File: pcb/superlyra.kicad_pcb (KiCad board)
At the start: 2 copper layers, 391.1 x 134.8 mm, 223 parts, among them J1 USB_C_Receptacle_USB2.0, J2 AVR-ISP-6, SW1 SW_Push, SW10 SW_Push, SW11 SW_Push, SW12 SW_Push, SW13 SW_Push, SW14 SW_Push, SW15 SW_Push, SW16 SW_Push, SW17 SW_Push, SW18 SW_Push, SW19 SW_Push, SW2 SW_Push, SW20 SW_Push, SW21 SW_Push, SW22 SW_Push, SW23 SW_Push, SW24 SW_Push, SW25 SW_Push, SW26 SW_Push, SW27 SW_Push, SW28 SW_Push, SW29 SW_Push, SW3 SW_Push, SW30 SW_Push, SW31 SW_Push, SW32 SW_Push, SW33 SW_Push, SW34 SW_Push, SW35 SW_Push, SW36 SW_Push, SW37 SW_Push, SW38 SW_Push, SW39 SW_Push, SW4 SW_Push, SW40 SW_Push, SW41 SW_Push, SW42 SW_Push, SW43 SW_Push, SW44 SW_Push, SW45 SW_Push, SW46 SW_Push, SW47 SW_Push, SW48 SW_Push, SW49 SW_Push, SW5 SW_Push, SW50 SW_Push, SW51 SW_Push, SW52 SW_Push, SW53 SW_Push, SW54 SW_Push, SW55 SW_Push, SW56 SW_Push, SW57 SW_Push, SW58 SW_Push, SW59 SW_Push, SW6 SW_Push, SW60 SW_Push, SW61 SW_Push, SW62 SW_Push, SW63 SW_Push, SW64 SW_Push, SW65 SW_Push, SW66 SW_Push, SW67 SW_Push, SW68 SW_Push, SW69 SW_Push, SW7 SW_Push, SW70 SW_Push, SW71 SW_Push, SW72 SW_Push, SW73 SW_Push, SW74 SW_Push, SW75 SW_Push, SW76 SW_Push, SW77 SW_Push, SW78 SW_Push, SW79 SW_Push, SW8 SW_Push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

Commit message: 0.5 (evaluation)
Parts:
- removed G***: LOGO, gfx:SuperLyraLogo
- removed REF** (x23): MountingHole_2.1mm, MountingHole:MountingHole_2.1mm
- removed the SW85 at (297.0, 165.2)
- added C6: 0.1u, Keebio:C_0402, F.Cu at (232.3, 87.1)
- added H1: MountingHole, MountingHole:MountingHole_2.2mm_M2_ISO7380_Pad, F.Cu at (59.7, 68.8)
- added H10: MountingHole, MountingHole:MountingHole_2.2mm_M2_ISO7380_Pad, F.Cu at (165.7, 84.3)
- added H11: MountingHole, MountingHole:MountingHole_2.2mm_M2_ISO7380_Pad, F.Cu at (256.4, 84.1)
- added H12: MountingHole, MountingHole:MountingHole_2.2mm_M2_ISO7380_Pad, F.Cu at (252.0, 121.3)
- added H13: MountingHole, MountingHole:MountingHole_2.2mm_M2_ISO7380_Pad, F.Cu at (255.4, 156.8)
- added H14: MountingHole, MountingHole:MountingHole_2.2mm_M2_ISO7380_Pad, F.Cu at (323.3, 78.9)
- added H15: MountingHole, MountingHole:MountingHole_2.2mm_M2_ISO7380_Pad, F.Cu at (247.9, 187.2)
- added H16: MountingHole, MountingHole:MountingHole_2.2mm_M2_ISO7380_Pad, F.Cu at (308.4, 170.8)
- added H17: MountingHole, MountingHole:MountingHole_2.2mm_M2_ISO7380_Pad, F.Cu at (335.3, 125.1)
- added H18: MountingHole, MountingHole:MountingHole_2.2mm_M2_ISO7380_Pad, F.Cu at (191.0, 142.1)
- added H19: MountingHole, MountingHole:MountingHole_2.2mm_M2_ISO7380_Pad, F.Cu at (291.7, 108.2)
- added H2: MountingHole, MountingHole:MountingHole_2.2mm_M2_ISO7380_Pad, F.Cu at (37.1, 153.9)
- added H20: MountingHole, MountingHole:MountingHole_2.2mm_M2_ISO7380_Pad, F.Cu at (360.4, 69.6)
- added H21: MountingHole, MountingHole:MountingHole_2.2mm_M2_ISO7380_Pad, F.Cu at (209.9, 163.6)
- added H22: MountingHole, MountingHole:MountingHole_2.2mm_M2_ISO7380_Pad, F.Cu at (229.1, 142.0)
- added H23: MountingHole, MountingHole:MountingHole_2.2mm_M2_ISO7380_Pad, F.Cu at (382.9, 154.7)
- added H24: MountingHole, MountingHole:MountingHole_2.2mm_M2_ISO7380_Pad, F.Cu at (209.9, 125.6)
- added H25: Logo, gfx:SuperLyraLogo, F.Cu at (181.4, 84.3)
- added H3: MountingHole, MountingHole:MountingHole_2.2mm_M2_ISO7380_Pad, F.Cu at (96.5, 79.5)
- added H4: MountingHole, MountingHole:MountingHole_2.2mm_M2_ISO7380_Pad, F.Cu at (84.8, 125.2)
- added H5: MountingHole, MountingHole:MountingHole_2.2mm_M2_ISO7380_Pad, F.Cu at (111.0, 170.4)
- added H6: MountingHole, MountingHole:MountingHole_2.2mm_M2_ISO7380_Pad, F.Cu at (128.0, 108.2)
- added H7: MountingHole, MountingHole:MountingHole_2.2mm_M2_ISO7380_Pad, F.Cu at (168.0, 121.2)
- added H8: MountingHole, MountingHole:MountingHole_2.2mm_M2_ISO7380_Pad, F.Cu at (165.0, 156.6)
- added H9: MountingHole, MountingHole:MountingHole_2.2mm_M2_ISO7380_Pad, F.Cu at (172.0, 187.3)
- D1, D10, D11, D12, D13, D14, D15, D16, D17, D18, D19, D2, D20, D21, D22, D23, D24, D25, D26, D27, D28, D29, D3, D30, D31, D32, D33, D34, D35, D36, D37, D38, D39, D4, D40, D41, D42, D43, D44, D45, D46, D47, D48, D49, D5, D50, D51, D52, D53, D54, D55, D56, D57, D58, D59, D6, D60, D61, D62, D63, D64, D65, D66, D67, D68, D69, D7, D70, D71, D72, D73, D74, D75, D76, D77, D78, D79, D8, D80, D81, D82, D83, D84, D85, D86, D87, D88, D89, D9, D90: footprint Keebio:D_0805 -> Diode_SMD:D_SOD-123F
- F1: footprint Fuse:Fuse_1206_3216Metric -> Fuse:Fuse_0402_1005Metric
- Y1: footprint Crystal:Resonator_SMD_muRata_CSTxExxV-3Pin_3.0x1.1mm_HandSoldering -> Crystal:Resonator_SMD_muRata_CSTxExxV-3Pin_3.0x1.1mm
- moved F1 19.3 mm to (228.6, 80.8)
- moved C1 8.62 mm to (235.7, 78.2), turned to 90 degrees
- moved R2 7.64 mm to (232.2, 79.2)
- moved R1 7.64 mm to (232.2, 80.3)
- moved C2 6.11 mm to (237.5, 78.2), turned to 90 degrees
- moved R3 5.30 mm to (231.1, 86.0)
- moved C3 5.18 mm to (243.6, 85.1), turned to 0 degrees
- moved D3 4.71 mm to (94.1, 88.5), turned to 75 degrees
- moved R4 4.66 mm to (243.6, 86.1), turned to 180 degrees
- moved C5 4.23 mm to (232.2, 81.5), turned to 180 degrees
- moved U2 3.84 mm to (218.4, 82.3), turned to 0 degrees
- moved J2 3.81 mm to (198.4, 83.3), turned to 180 degrees
- moved D21 3.42 mm to (92.8, 93.1), turned to 255 degrees
- moved C4 3.39 mm to (237.5, 90.2)
- moved D12 3.20 mm to (270.1, 101.8), turned to 105 degrees
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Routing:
- net GND: track 88.7 -> 43.5 mm, vias 34 -> 17
- net COL16: track 183.9 -> 150.0 mm
- net COL15: track 165.6 -> 133.2 mm
- net ROW3: track 520.8 -> 491.1 mm, vias 4 -> 3
- net MISO: track 469.7 -> 443.0 mm, vias 4 -> 2
- net MOSI: track 490.4 -> 467.6 mm
- net COL11: track 99.2 -> 79.8 mm
- net ROW0: track 402.5 -> 386.0 mm
- net COL14: track 143.2 -> 128.2 mm
- net /D-: track 18.9 -> 4.23 mm
- net /D+: track 18.4 -> 3.86 mm
- net COL13: track 120.6 -> 107.1 mm
- net /vbus-in: track 14.8 -> 26.6 mm, vias 0 -> 2
- net Net-(C1-Pad1): track 15.2 -> 5.69 mm
- net Net-(D12-Pad2): track 20.2 -> 11.1 mm
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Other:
- board text added: "github.com/Malevolti/SuperLyra ver. 0.5 (evaluation) youtu.be/8CP6Chss0y0"
- board text removed: "github.com/Malevolti/SuperLyra ver. 1.0 youtu.be/8CP6Chss0y0 Special thanks to Pat for know more about capacitors than me."

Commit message: Update superlyra.kicad_pcb
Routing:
- net VCC: track 110.5 -> 108.0 mm
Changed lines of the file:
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@@
     (thickness 1.6)
     (drawings 20)
-    (tracks 1141)
+    (tracks 1136)
     (zones 0)
     (modules 224)
@@
     (tags "resistor handsolder")
     (attr smd)
-    (fp_text reference R3 (at 0 0.889 90) (layer F.SilkS)
+    (fp_text reference R3 (at -1.651 0 180) (layer F.SilkS)
       (effects (font (size 0.7 0.7) (thickness 0.15)))
     )
@@
     (tags "resistor handsolder")
     (attr smd)
-    (fp_text reference R4 (at 0 -1.17) (layer F.SilkS)
-      (effects (font (size 1 1) (thickness 0.15)))
+    (fp_text reference R4 (at 0 -1.143) (layer F.SilkS)
+      (effects (font (size 0.7 0.7) (thickness 0.15)))
     )
     (fp_text value 10k (at 0 1.17) (layer F.Fab)
@@
     (tags "capacitor 0402")
     (attr smd)
-    (fp_text reference C6 (at 0 -1.016 90) (layer F.SilkS)
+    (fp_text reference C6 (at 1.651 0 180) (layer F.SilkS)
       (effects (font (size 0.7 0.7) (thickness 0.15)))
     )
@@
   (segment (start 233.33668 86.614) (end 232.198 86.614) (width 0.25) (layer F.Cu) (net 3))
   (segment (start 234.069371 85.881309) (end 233.33668 86.614) (width 0.25) (layer F.Cu) (net 3))
-  (segment (start 227.584 82.296) (end 220.98 82.296) (width 0.25) (layer B.Cu) (net 3))
   (segment (start 220.98 82.296) (end 220.98 82.296) (width 0.25) (layer B.Cu) (net 3))
   (via (at 220.98 82.296) (size 0.8) (drill 0.4) (layers F.Cu B.Cu) (net 3))
@@
   (segment (start 235.204 90.17) (end 234.78 90.17) (width 0.25) (layer B.Cu) (net 3))
   (segment (start 239.014 90.17) (end 235.204 90.17) (width 0.25) (layer B.Cu) (net 3))
-  (segment (start 239.48 78.782) (end 238.676 77.978) (width 0.25) (layer B.Cu) (net 3))
-  (segment (start 238.676 77.978) (end 231.902 77.978) (width 0.25) (layer B.Cu) (net 3))
-  (segment (start 230.632 79.248) (end 231.775 78.105) (width 0.25) (layer B.Cu) (net 3))
-  (segment (start 231.775 78.105) (end 231.902 77.978) (width 0.25) (layer B.Cu) (net 3))
-  (segment (start 228.219 80.518) (end 228.219 81.661) (width 0.25) (layer B.Cu) (net 3))
-  (segment (start 228.219 80.518) (end 228.219 79.248) (width 0.25) (layer B.Cu) (net 3))
-  (segment (start 228.219 79.248) (end 230.632 79.248) (width 0.25) (layer B.Cu) (net 3))
-  (segment (start 227.584 82.296) (end 228.219 82.296) (width 0.25) (layer B.Cu) (net 3))
-  (segment (start 228.219 81.661) (end 228.219 82.296) (width 0.25) (layer B.Cu) (net 3))
-  (segment (start 228.219 82.296) (end 228.219 82.804) (width 0.25) (layer B.Cu) (net 3))
-  (segment (start 228.219 82.804) (end 228.219 83.058) (width 0.25) (layer B.Cu) (net 3))
   (segment (start 231.1445 86.572) (end 231.14 86.5765) (width 0.25) (layer F.Cu) (net 3))
   (segment (start 232.283 86.572) (end 231.1445 86.572) (width 0.25) (layer F.Cu) (net 3))
   (segment (start 230.0345 86.5765) (end 229.997 86.614) (width 0.25) (layer F.Cu) (net 3))
   (segment (start 231.14 86.5765) (end 230.0345 86.5765) (width 0.25) (layer F.Cu) (net 3))
-  (segment (start 229.997 86.614) (end 231.521 86.614) (width 0.25) (layer B.Cu) (net 3))
-  (segment (start 231.521 86.614) (end 232.156 85.979) (width 0.25) (layer B.Cu) (net 3))
-  (segment (start 232.156 85.979) (end 232.156 84.709) (width 0.25) (layer B.Cu) (net 3))
-  (segment (start 232.156 84.709) (end 231.648 84.201) (width 0.25) (layer B.Cu) (net 3))
-  (segment (start 229.235 84.201) (end 228.219 83.185) (width 0.25) (layer B.Cu) (net 3))
-  (segment (start 231.648 84.201) (end 229.235 84.201) (width 0.25) (layer B.Cu) (net 3))
-  (segment (start 228.219 82.804) (end 228.219 83.185) (width 0.25) (layer B.Cu) (net 3))
   (segment (start 229.1715 80.7085) (end 229.108 80.772) (width 0.25) (layer F.Cu) (net 3))
   (segment (start 231.072999 80.958999) (end 230.8225 80.7085) (width 0.25) (layer F.Cu) (net 3))
@@
   (segment (start 228.6 81.788) (end 228.6 81.788) (width 0.25) (layer F.Cu) (net 3))
   (via (at 228.6 81.788) (size 0.8) (drill 0.4) (layers F.Cu B.Cu) (net 3))
-  (segment (start 228.346 81.788) (end 228.219 81.661) (width 0.25) (layer B.Cu) (net 3))
   (segment (start 228.6 81.788) (end 228.346 81.788) (width 0.25) (layer B.Cu) (net 3))
-  (segment (start 210.85498 80.04498) (end 227.42202 80.04498) (width 0.25) (layer B.Cu) (net 3))
-  (segment (start 227.42202 80.04498) (end 228.219 79.248) (width 0.25) (layer B.Cu) (net 3))
   (segment (start 210.579989 79.769989) (end 210.85498 80.04498) (width 0.25) (layer B.Cu) (net 3))
   (segment (start 204.456011 79.769989) (end 210.579989 79.769989) (width 0.25) (layer B.Cu) (net 3))
   (segment (start 200.914 83.312) (end 204.456011 79.769989) (width 0.25) (layer B.Cu) (net 3))
+  (segment (start 229.071001 82.259001) (end 228.6 81.788) (width 0.25) (layer B.Cu) (net 3))
+  (segment (start 236.002999 82.259001) (end 229.071001 82.259001) (width 0.25) (layer B.Cu) (net 3))
+  (segment (start 239.48 78.782) (end 236.002999 82.259001) (width 0.25) (layer B.Cu) (net 3))
+  (segment (start 226.85698 80.04498) (end 225.13602 80.04498) (width 0.25) (layer B.Cu) (net 3))
+  (segment (start 228.6 81.788) (end 226.85698 80.04498) (width 0.25) (layer B.Cu) (net 3))
+  (segment (start 210.85498 80.04498) (end 225.13602 80.04498) (width 0.25) (layer B.Cu) (net 3))
+  (segment (start 228.092 82.296) (end 226.949 82.296) (width 0.25) (layer B.Cu) (net 3))
+  (segment (start 226.949 82.296) (end 220.98 82.296) (width 0.25) (layer B.Cu) (net 3))
+  (segment (start 227.584 82.296) (end 226.949 82.296) (width 0.25) (layer B.Cu) (net 3))
+  (segment (start 228.6 81.788) (end 228.092 82.296) (width 0.25) (layer B.Cu) (net 3))
+  (segment (start 229.235 84.201) (end 228.6 83.566) (width 0.25) (layer B.Cu) (net 3))
+  (segment (start 230.759 84.201) (end 229.235 84.201) (width 0.25) (layer B.Cu) (net 3))
+  (segment (start 231.14 84.582) (end 230.759 84.201) (width 0.25) (layer B.Cu) (net 3))
+  (segment (start 231.14 86.233) (end 231.14 84.582) (width 0.25) (layer B.Cu) (net 3))
+  (segment (start 228.6 83.566) (end 228.6 81.788) (width 0.25) (layer B.Cu) (net 3))
+  (segment (start 230.759 86.614) (end 231.14 86.233) (width 0.25) (layer B.Cu) (net 3))
+  (segment (start 229.997 86.614) (end 230.759 86.614) (width 0.25) (layer B.Cu) (net 3))
   (segment (start 229.486 110.112) (end 246.888 110.112) (width 0.25) (layer F.Cu) (net 4))
   (via (at 229.486 110.112) (size 0.8) (drill 0.4) (layers F.Cu B.Cu) (net 4))
@@
   (segment (start 221.46697 88.07188) (end 203.13388 88.07188) (width 0.25) (layer F.Cu) (net 61))
   (segment (start 201.168 86.106) (end 201.93 86.868) (width 0.25) (layer F.Cu) (net 61))
-  (segment (start 233.53269 82.74601) (end 234.069371 83.282691) (width 0.25) (layer F.Cu) (net 61))
-  (segment (start 231.689619 83.268971) (end 232.21258 82.74601) (width 0.25) (layer F.Cu) (net 61))
-  (segment (start 232.21258 82.74601) (end 233.53269 82.74601) (width 0.25) (layer F.Cu) (net 61))
-  (segment (start 226.269879 83.268971) (end 231.689619 83.268971) (width 0.25) (layer F.Cu) (net 61))
-  (segment (start 222.650925 86.887925) (end 226.269879 83.268971) (width 0.25) (layer F.Cu) (net 61))
   (segment (start 102.470347 130.219704) (end 101.028643 128.778) (width 0.25) (layer F.Cu) (net 61))
   (segment (start 83.846051 128.778) (end 82.912347 129.711704) (width 0.25) (layer F.Cu) (net 61))
@@
   (segment (start 193.548 149.86) (end 193.17 150.238) (width 0.25) (layer B.Cu) (net 61))
   (segment (start 191.262 138.43) (end 193.548 140.716) (width 0.25) (layer B.Cu) (net 61))
+  (segment (start 233.53269 82.74601) (end 234.069371 83.282691) (width 0.25) (layer F.Cu) (net 61) (status 1000000))
+  (segment (start 226.269879 83.268971) (end 231.689619 83.268971) (width 0.25) (layer F.Cu) (net 61) (status 1000000))
+  (segment (start 232.21258 82.74601) (end 233.53269 82.74601) (width 0.25) (layer F.Cu) (net 61) (status 1000000))
+  (segment (start 222.650925 86.887925) (end 226.269879 83.268971) (width 0.25) (layer F.Cu) (net 61) (status 1000000))
+  (segment (start 231.689619 83.268971) (end 232.21258 82.74601) (width 0.25) (layer F.Cu) (net 61) (status 1000000))
   (segment (start 280.706066 144.989296) (end 276.879042 148.81632) (width 0.25) (layer F.Cu) (net 73))
   (segment (start 281.667347 144.989296) (end 280.706066 144.989296) (width 0.25) (layer F.Cu) (net 73))

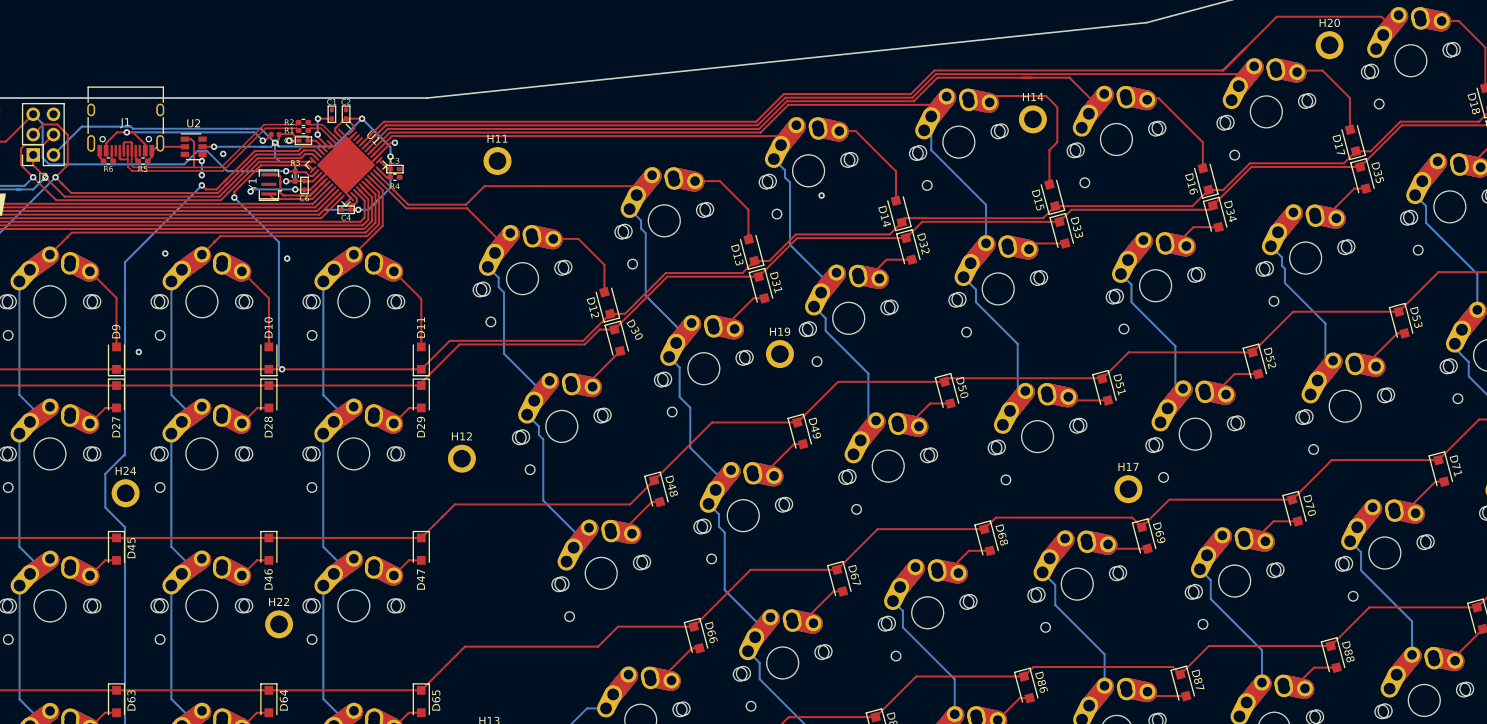
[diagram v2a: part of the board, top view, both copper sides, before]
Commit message: fixed missing connectons on some of the columns
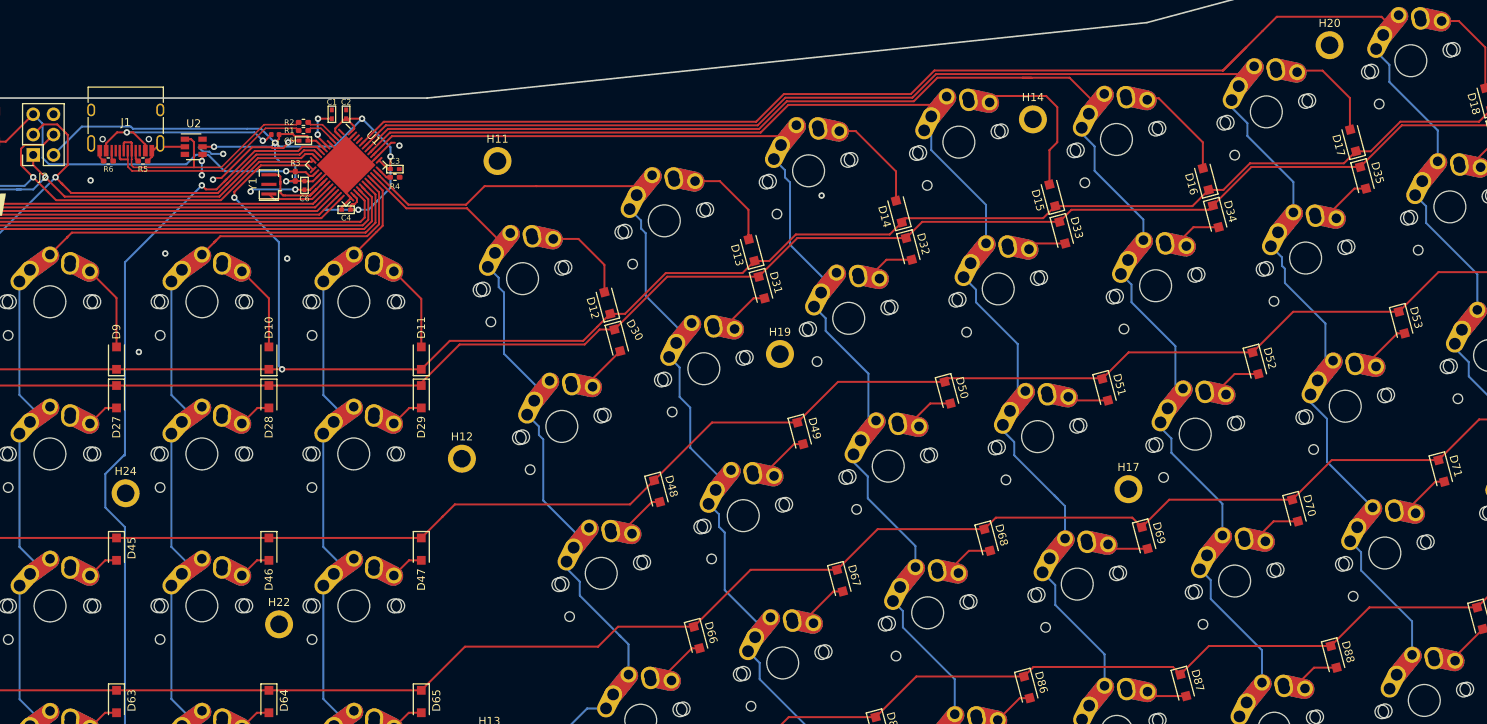
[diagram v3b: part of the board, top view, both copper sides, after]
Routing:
- net COL15: track 133.2 -> 167.8 mm
- net COL16: track 150.0 -> 184.5 mm
- net COL14: track 128.2 -> 146.1 mm
- net COL11: track 79.8 -> 97.5 mm
- net COL13: track 107.1 -> 124.4 mm
- net COL17: track 194.3 -> 211.5 mm
- net GND: track 43.5 -> 57.9 mm, vias 17 -> 19
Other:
- net class Default: clearance 0.2 -> 0.127
- rule trace_clearance: 0.2 -> 0.127
- rule trace_min: 0.2 -> 0.127
